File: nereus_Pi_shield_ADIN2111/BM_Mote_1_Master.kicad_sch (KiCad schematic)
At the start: 42 parts, among them P1 DF17(3.0)-30DS-0.5V(57)

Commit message: S2.1: delete the mezzanine (P1, R9, 12 TPs, 14 labels, orphan power symbols/NCs/wires)
tools/schedit.py: tested sheet edits (delete with island cleanup, add symbol/
wire/label/NC). Kept-part connectivity verified identical before/after.
ERC 65/590 -> 48/562; netcheck 53/53, 0 parts excluded.

Co-Authored-By: Claude Opus 5.5 <noreply@anthropic.com>
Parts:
- removed P1: DF17(3.0)-30DS-0.5V(57), FP-DF17_3_0H_-30DS-0_5V_5-MFG, symbol BM_Mote_000639-AB-altium-import:Designator_0_mirrored_c198d1f49c97548841516d61f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
- removed R9: RC0402JR-070RL, RESC1005X40X25NL05T10, symbol BM_Mote_000639-AB-altium-import:Designator_0_RES_Altium Content Vault_0
- removed TP10, TP11, TP12, TP14, TP15, TP16, TP17, TP18, TP4, TP6, TP9: TEST_POINT, PCB_TP_1.5mm, symbol BM_Mote_000639-AB-altium-import:Designator_2_TEST_POINT_Sofar Ocean Technologie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
- removed TP33: TEST_POINT, PCB_TP_1.5mm, symbol BM_Mote_000639-AB-altium-import:Designator_0_TEST_POINT_Sofar Ocean Technologie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
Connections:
- no-connect marks 2 -> 0

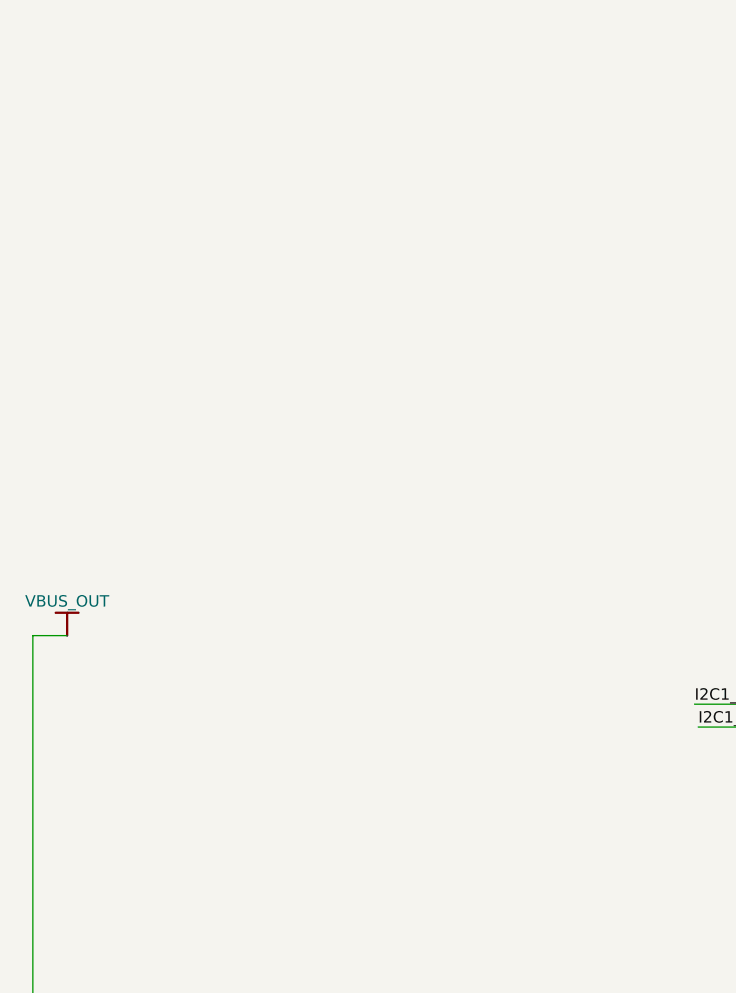
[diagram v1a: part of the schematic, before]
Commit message: S2.2: place Pi header J1 with GND, PWR_FLAGs and 3V3 no-connect; S2 docs
- J1 Connector:Raspberry_Pi_2_3 (KiCad 9.0.6 library), footprint
  PinSocket_2x20_P2.54mm_Vertical, at (121.92, 88.9) in clear space.
- All 8 GND pins on GND (one symbol at the stacked pin point, verified in
  the netlist); NC flag on pins 1/17 (Pi 3V3); PWR_FLAG on GND and VBUS.
- schedit: wires carrying a label part-way are shortened, not deleted
  (keeps the I2C1 labels; test added). next_ref keeps zero-padding.
- Changelog, TRACKER, DESIGN (ERC owners), SPEC (I2C pull-up question),
  DEV_LOG and checklist HTML synced.

Co-Authored-By: Claude Opus 5.5 <noreply@anthropic.com>
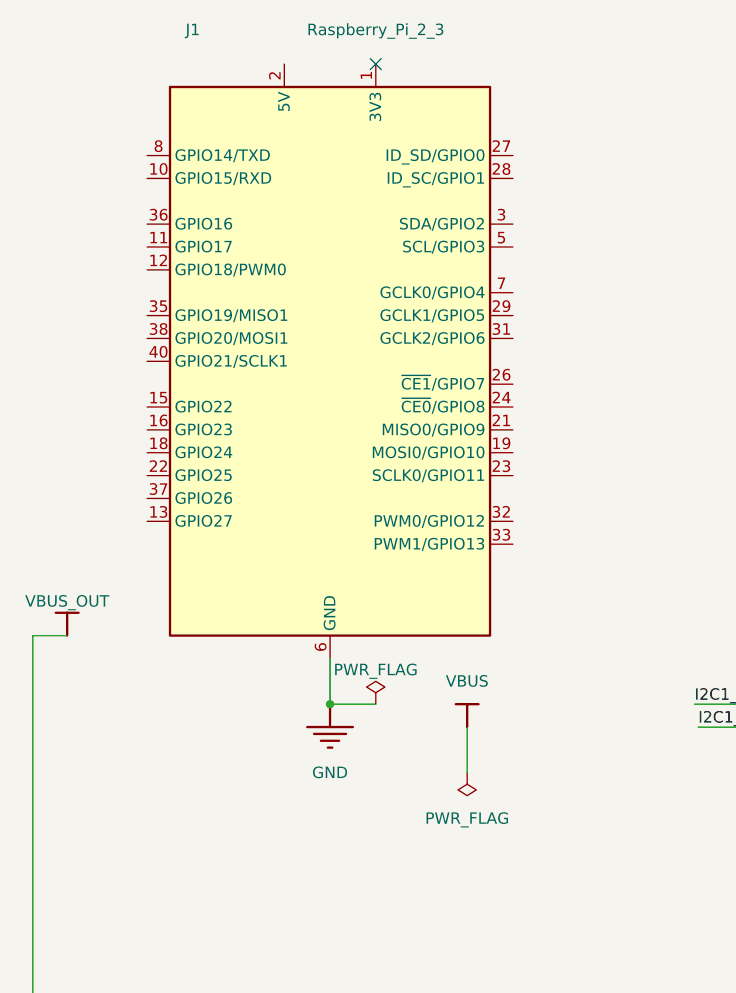
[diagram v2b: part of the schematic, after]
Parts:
- added J1: Raspberry_Pi_2_3, Connector_PinSocket_2.54mm:PinSocket_2x20_P2.54mm_Vertical, symbol Connector:Raspberry_Pi_2_3
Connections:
- net GND: now also J1.14 (GND), J1.20 (GND), J1.25 (GND), J1.30 (GND), J1.34 (GND), J1.39 (GND), J1.6 (GND), J1.9 (GND)
- new net: J1.1 (3V3), J1.17 (3V3)
- new net: J1.2 (5V), J1.4 (5V)
- no-connect marks 0 -> 1
